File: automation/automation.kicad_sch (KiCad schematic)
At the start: 11 parts, among them J1 Raspberry_Pi_2_3, J2 Relay 6 pin, J3 Relay 2pin, Q1 BC546B, Q2 BC546B, Q3 BC546B, Q4 BC546B

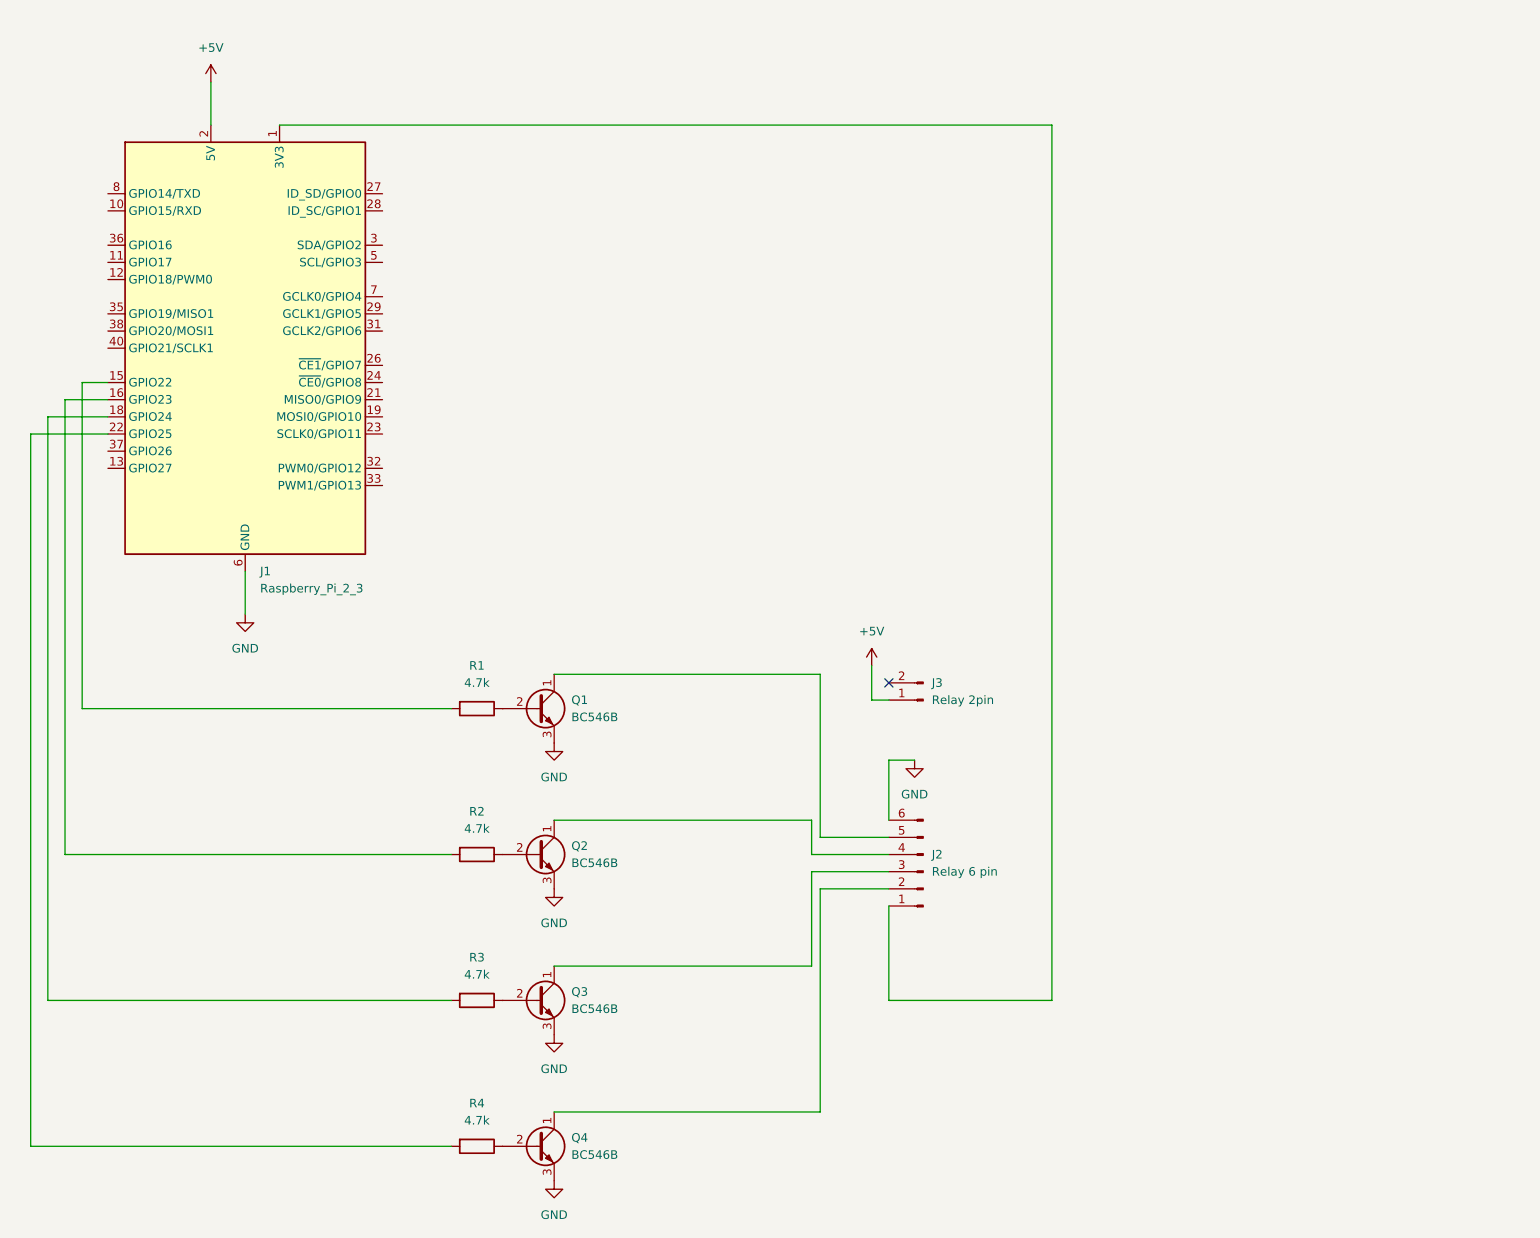
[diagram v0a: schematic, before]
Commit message: Update the relay circuit and add the distance sensor
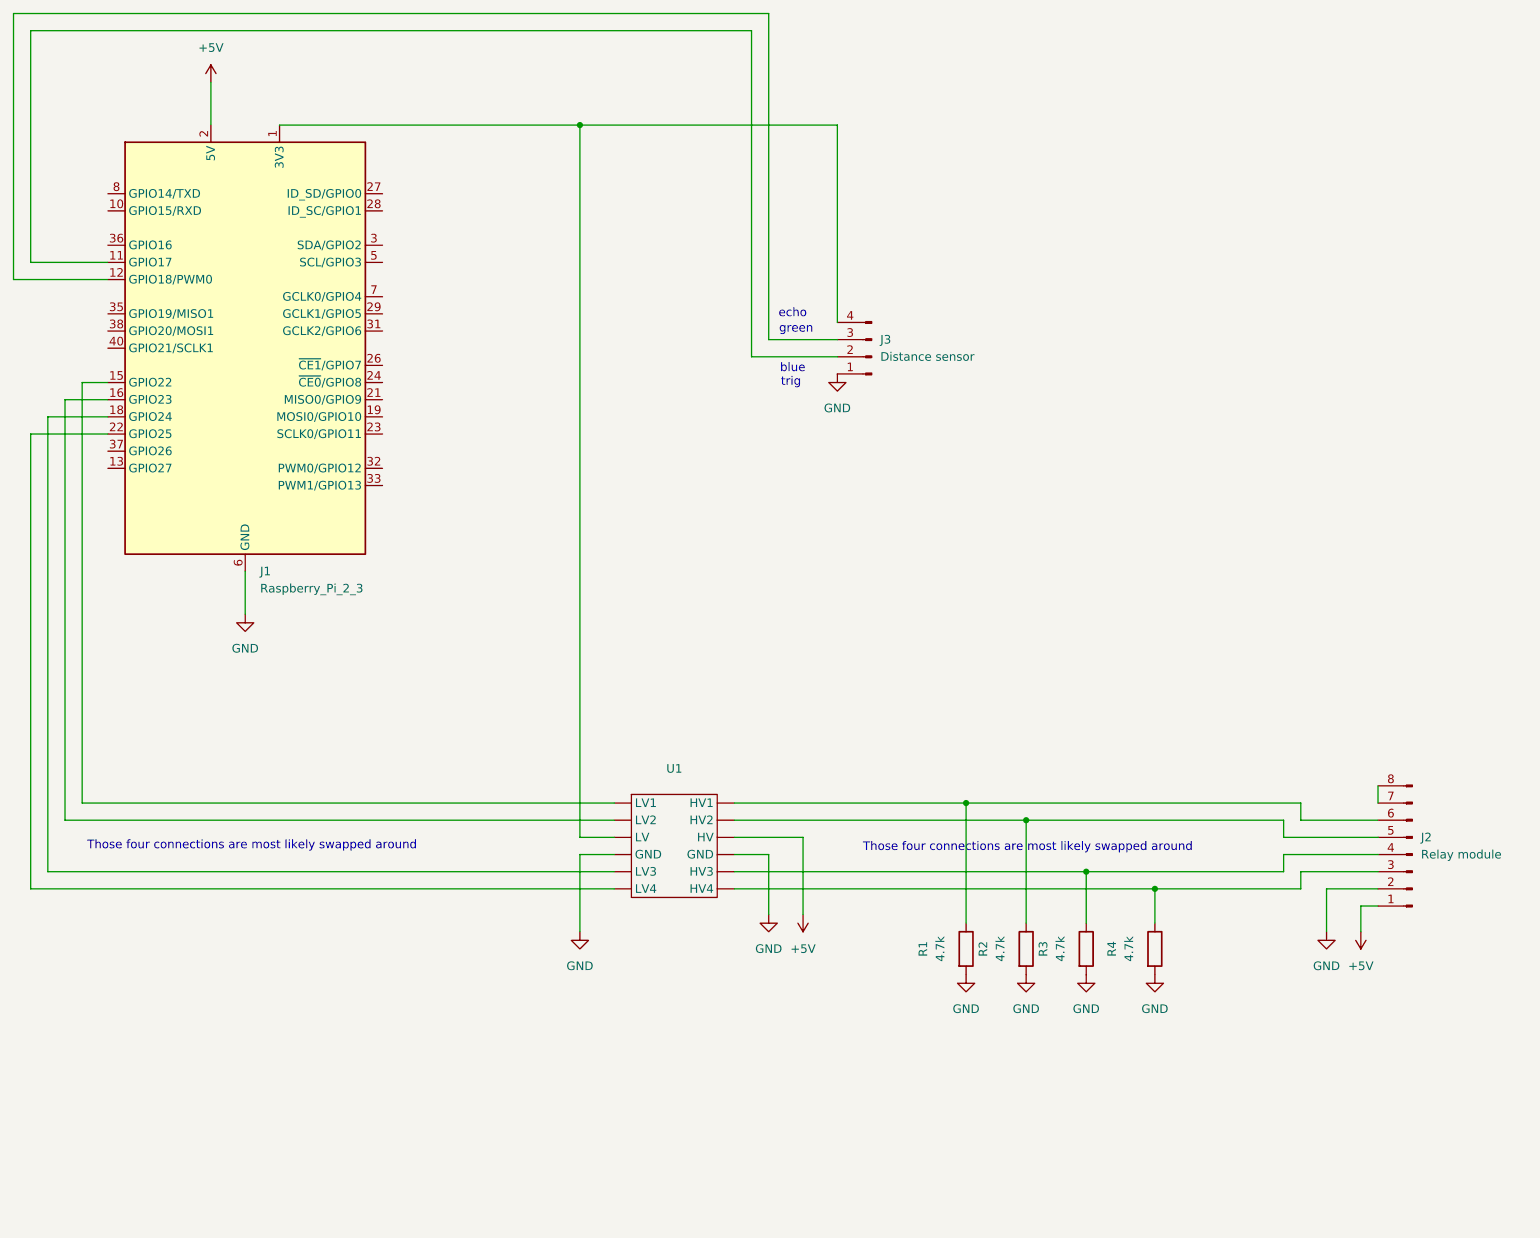
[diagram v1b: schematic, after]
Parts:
- removed J2: Relay 6 pin, symbol Connector:Conn_01x06_Pin
- removed J3: Relay 2pin, symbol Connector:Conn_01x02_Pin
- removed Q1, Q2, Q3, Q4: BC546B, Package_TO_SOT_THT:TO-92_Inline, symbol Transistor_BJT:BC546
- added J2: Relay module, symbol Connector:Conn_01x08_Pin
- added J3: Distance sensor, symbol Connector:Conn_01x04_Pin
- added U1: ~, symbol custom:level_converter
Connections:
- net +5V: now also J2.1 (Pin_1), U1. (LV4)
- net GND: now also R1.2, R2.2, R3.2, R4.2, J2.2 (Pin_2), J3.1 (Pin_1), U1. (LV4)
- net at R3.1: now also J2.4 (Pin_4), U1. (LV4)
- net at J1.18 (GPIO24): now also U1. (LV4); no longer R3.2
- net at R4.1: now also J2.3 (Pin_3), U1. (LV4)
- net at J1.22 (GPIO25): now also U1. (LV4); no longer R4.2
- net at J1.1 (3V3), J1.17 (3V3): now also J3.4 (Pin_4), U1. (LV4)
- net at R2.1: now also J2.5 (Pin_5), U1. (LV4)
- net at J1.16 (GPIO23): now also U1. (LV4); no longer R2.2
- net at R1.1: now also J2.6 (Pin_6), U1. (LV4)
- net at J1.15 (GPIO22): now also U1. (LV4); no longer R1.2
- net at J1.11 (GPIO17): now also J3.2 (Pin_2)
- net at J1.12 (GPIO18/PWM0): now also J3.3 (Pin_3)
- new net: J2.7 (Pin_7), J2.8 (Pin_8)
- no-connect marks 1 -> 0
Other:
- note added: "Those four connections are most likely swapped around"
- note added: "blue"
- note added: "echo"
- note added: "green"
- note added: "trig"
- moved on the sheet: R1, R2, R3, R4

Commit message: Add HTP
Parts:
- added J4: HTP sensor (AHT20+BMP280), symbol Connector:Conn_01x04_Pin
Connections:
- net GND: now also J4.1 (Pin_1)
- net at J1.1 (3V3), J1.17 (3V3), J3.4 (Pin_4)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: now also J4.2 (Pin_2)
- net at J1.3 (SDA/GPIO2): now also J4.4 (Pin_4)
- net at J1.5 (SCL/GPIO3): now also J4.3 (Pin_3)
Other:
- note added: "does not correspond to the order on the package"
- note added: "red vcc black gnd white sda green scl"

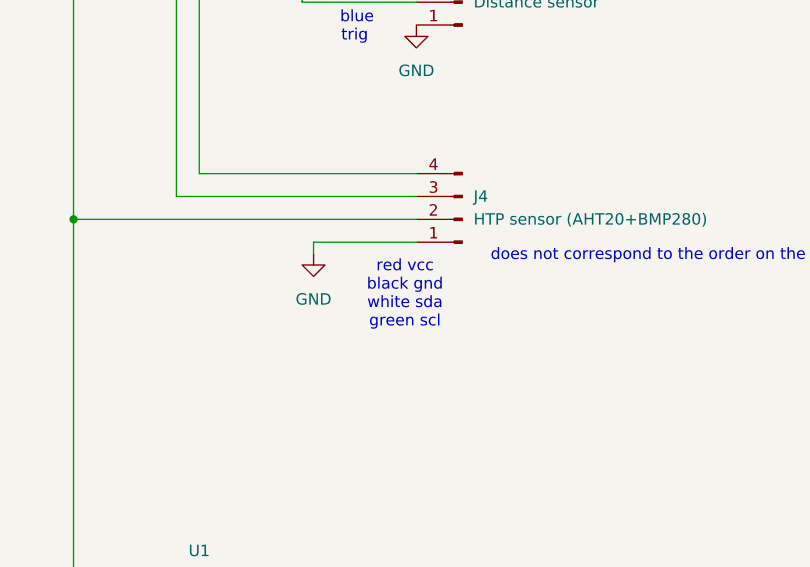
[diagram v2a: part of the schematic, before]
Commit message: Correct cable colors
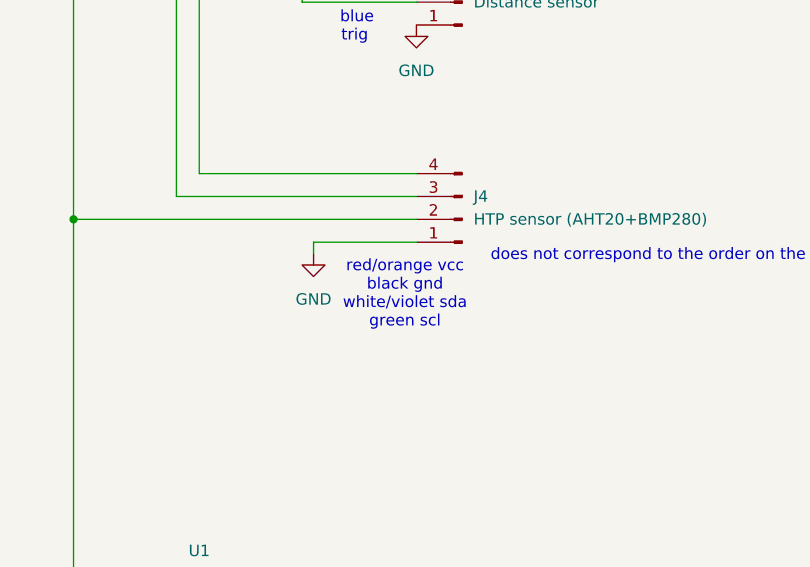
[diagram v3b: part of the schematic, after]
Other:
- note added: "red/orange vcc black gnd white/violet sda green scl"
- note removed: "red vcc black gnd white sda green scl"
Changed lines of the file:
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@@
 		)
 	)
-	(text "red vcc\nblack gnd\nwhite sda\ngreen scl"
+	(text "red/orange vcc\nblack gnd\nwhite/violet sda\ngreen scl"
 		(exclude_from_sim no)
 		(at 133.35 96.012 0)
